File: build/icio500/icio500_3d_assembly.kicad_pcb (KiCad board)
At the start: 4 copper layers, 150.8 x 114.3 mm, 57 parts, among them J1 ?, U1 ?, U2 ?, U3 ?, U4 ?, U5 ?, U6 ?

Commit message: idk
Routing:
- net audio_in_r: track 108.5 -> 19.5 mm, vias 3 -> 0
- net gpio_disp_dc: track 76.4 -> 0.76 mm, vias 3 -> 0
- net gnd: track 235.5 -> 160.7 mm, vias 25 -> 22
- net i2c1_scl: track 74.9 -> 1.02 mm, vias 3 -> 0
- net gpio_disp_res: track 76.9 -> 3.48 mm, vias 3 -> 0
- net spi1_sck: track 69.8 -> 0.00 mm, vias 3 -> 0
- net i2c1_sda: track 70.3 -> 0.73 mm, vias 3 -> 0
- net spi1_cs: track 69.8 -> 0.98 mm, vias 3 -> 0
- net spi1_mosi: track 67.8 -> 1.14 mm, vias 3 -> 0
- net spi1_miso: track 63.7 -> 2.81 mm, vias 3 -> 0
- net gpio_enc_b: track 59.1 -> 30.5 mm, vias 3 -> 1
- net gpio_enc_sw: track 60.0 -> 34.9 mm, vias 3 -> 1
- net d13: track 55.7 -> 32.4 mm, vias 3 -> 1
- net d14: track 56.4 -> 33.7 mm, vias 3 -> 1
- net daisy_5v_power: track 155.1 -> 133.7 mm, vias 3 -> 1

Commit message: multistep error check and fixing
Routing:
- net i2c1_sda: track 0.73 -> 124.5 mm, vias 0 -> 3
- net i2c1_scl: track 1.02 -> 122.5 mm, vias 0 -> 3
- net spi1_mosi: track 1.14 -> 115.4 mm, vias 0 -> 3
- net spi1_sck: track 0.00 -> 114.0 mm, vias 0 -> 3
- net gpio_disp_dc: track 0.76 -> 112.5 mm, vias 0 -> 3
- net spi1_cs: track 0.98 -> 106.9 mm, vias 0 -> 3
- net spi1_miso: track 2.81 -> 108.3 mm, vias 0 -> 3
- net gpio_disp_res: track 3.48 -> 105.4 mm, vias 0 -> 3
- net d13: track 32.4 -> 113.8 mm, vias 1 -> 3
- net gpio_enc_b: track 30.5 -> 110.2 mm, vias 1 -> 3
- net d14: track 33.7 -> 105.6 mm, vias 1 -> 3
- net gpio_enc_sw: track 34.9 -> 102.0 mm, vias 1 -> 3
- net audio_in_r: track 19.5 -> 86.1 mm, vias 0 -> 3
- net gnd: track 160.7 -> 127.7 mm, vias 22 -> 28
- net daisy_5v_power: track 133.7 -> 135.0 mm, vias 1 -> 2

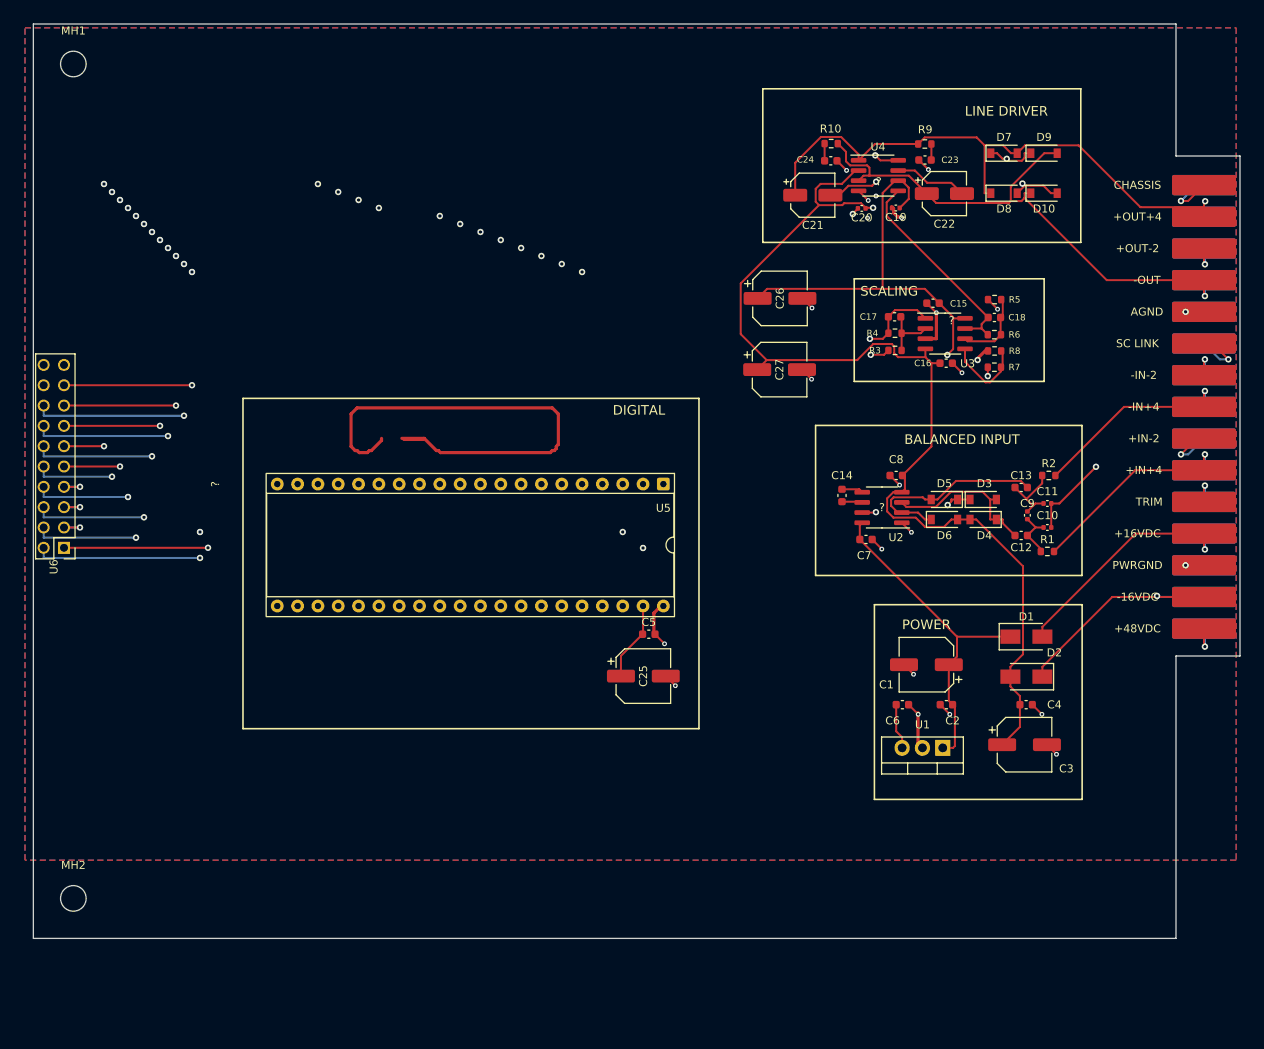
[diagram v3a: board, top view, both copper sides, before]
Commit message: Restore VPR summer board outline (Y=160mm, 26mm bottom notch), align lower bracket BR2, purge vestigial files
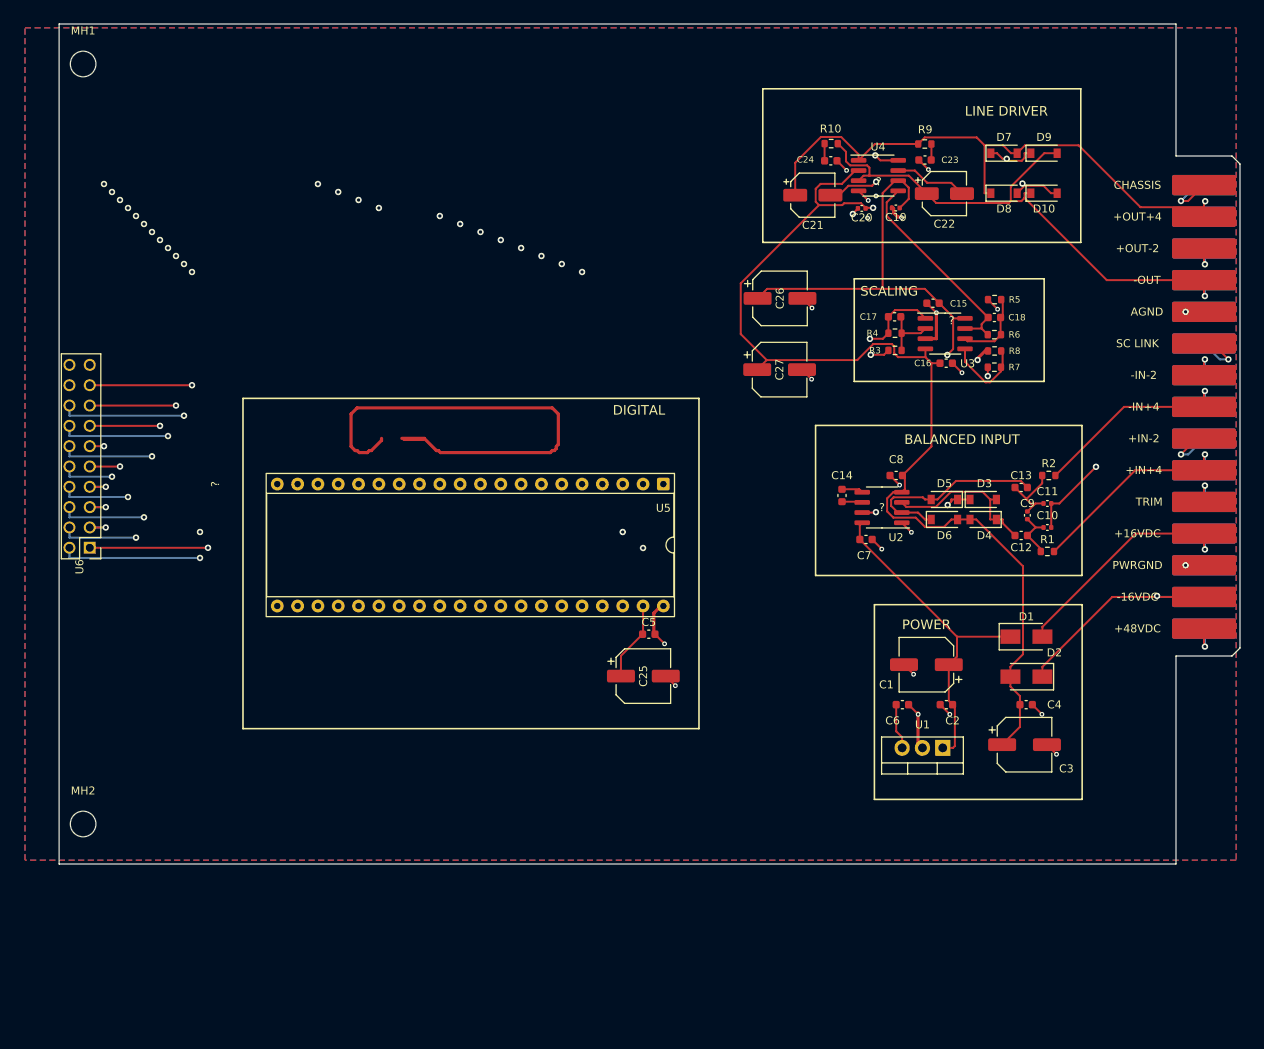
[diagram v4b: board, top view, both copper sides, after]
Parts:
- moved MH2 9.38 mm to (58.4, 155.0)
- moved U6 3.22 mm to (59.2, 120.5)
- moved ? 3.22 mm to (55.4, 112.2)
- moved MH1 1.22 mm to (58.4, 60.0)
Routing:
- net spi1_sck: track 114.0 -> 110.7 mm
- net spi1_mosi: track 115.4 -> 112.2 mm
- net spi1_miso: track 108.3 -> 105.1 mm
- net spi1_cs: track 106.9 -> 103.7 mm
- net i2c1_sda: track 124.5 -> 121.3 mm
- net i2c1_scl: track 122.5 -> 119.3 mm
- net gpio_enc_sw: track 102.0 -> 98.8 mm
- net gpio_enc_b: track 110.2 -> 107.0 mm
- net gpio_disp_res: track 105.4 -> 102.2 mm
- net daisy_5v_power: track 135.0 -> 131.8 mm
- net d14: track 105.6 -> 102.4 mm
- net d13: track 113.8 -> 110.6 mm
- net audio_in_r: track 86.1 -> 82.9 mm
- net gpio_disp_dc: track 112.5 -> 109.3 mm
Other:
- board size 150.8 x 114.3 mm -> 147.6 x 105 mm
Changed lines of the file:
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@@
 	(footprint "MountingHole_3.2mm_M3"
 		(layer "F.Cu")
-		(at 57.17 164.3)
+		(at 58.39 155)
 		(descr "Mounting Hole 3.2mm, M3, no annular, generated by kicad-footprint-generator mountinghole.py")
 		(tags "mountinghole M3")
@@
 	(footprint "Connector_PinHeader_2.54mm:PinHeader_2x10_P2.54mm_Horizontal"
 		(layer "F.Cu")
-		(at 56 120.475 180)
+		(at 59.22 120.47 180)
 		(descr "Through hole straight pin header, 2x10, 2.54mm pitch, double rows")
 		(tags "Through hole pin header THT 2x10 2.54mm double row")
@@
 	(footprint "MountingHole_3.2mm_M3"
 		(layer "F.Cu")
-		(at 57.17 60)
+		(at 58.39 60)
 		(descr "Mounting Hole 3.2mm, M3, no annular, generated by kicad-footprint-generator mountinghole.py")
 		(tags "mountinghole M3")
@@
 	)
 	(gr_line
-		(start 52.17 55)
+		(start 55.39 55)
 		(end 195 55)
 		(stroke
@@
 	)
 	(gr_line
-		(start 52.17 169.3)
-		(end 52.17 55)
+		(start 55.39 160)
+		(end 55.39 55)
 		(stroke
 			(width 0.1)
@@
 	(gr_line
 		(start 195 71.5)
-		(end 203 71.5)
+		(end 202 71.5)
 		(stroke
 			(width 0.1)
@@
 	(gr_line
 		(start 195 134)
-		(end 195 169.3)
+		(end 195 160)
 		(stroke
 			(width 0.1)
@@
 	)
 	(gr_line
-		(start 195 169.3)
-		(end 52.17 169.3)
+		(start 195 160)
+		(end 55.39 160)
 		(stroke
 			(width 0.1)
@@
 	)
 	(gr_line
-		(start 203 71.5)
-		(end 203 134)
+		(start 202 71.5)
+		(end 203 72.5)
 		(stroke
 			(width 0.1)
@@
 	)
 	(gr_line
-		(start 203 134)
+		(start 202 134)
 		(end 195 134)
 		(stroke
@@
 		(layer "Edge.Cuts")
 	)
+	(gr_line
+		(start 203 72.5)
+		(end 203 133)
+		(stroke
+			(width 0.1)
+			(type default)
+		)
+		(layer "Edge.Cuts")
+	)
+	(gr_line
+		(start 203 133)
+		(end 202 134)
+		(stroke
+			(width 0.1)
+			(type default)
+		)
+		(layer "Edge.Cuts")
+	)
 	(gr_text "DIGITAL"
 		(at 127.873162 103.2775 0)
@@
 	)
 	(segment
-		(start 56 120.475)
+		(start 59.22 120.475)
 		(end 74 120.475)
 		(width 0.25)
@@
 	)
 	(segment
-		(start 56 112.855)
-		(end 58 112.855)
+		(start 59.22 112.855)
+		(end 61.22 112.855)
 		(width 0.25)
 		(layer "F.Cu")
@@
 	)
 	(segment
-		(start 56 115.395)
-		(end 58 115.395)
+		(start 59.22 115.395)
+		(end 61.22 115.395)
 		(width 0.25)
 		(layer "F.Cu")
@@
 	)
 	(segment
-		(start 56 117.935)
-		(end 58 117.935)
+		(start 59.22 117.935)
+		(end 61.22 117.935)
 		(width 0.25)
 		(layer "F.Cu")
@@
 	)
 	(via
-		(at 58 117.935)
+		(at 61.22 117.935)
 		(size 0.8)
 		(drill 0.4)
@@
 	)
 	(via
-		(at 58 115.395)
+		(at 61.22 115.395)
 		(size 0.8)
 		(drill 0.4)
@@
 	)
 	(via
-		(at 58 112.855)
+		(at 61.22 112.855)
 		(size 0.8)
 		(drill 0.4)
@@
 	)
 	(segment
-		(start 56 115.395)
-		(end 58 115.395)
+		(start 59.22 115.395)
+		(end 61.22 115.395)
 		(width 0.25)
 		(layer "B.Cu")
@@
 	)
 	(segment
-		(start 56 112.855)
-		(end 58 112.855)
+		(start 59.22 112.855)
+		(end 61.22 112.855)
 		(width 0.25)
 		(layer "B.Cu")
@@
 	)
 	(segment
-		(start 56 117.935)
-		(end 58 117.935)
+		(start 59.22 117.935)
+		(end 61.22 117.935)
 		(width 0.25)
 		(layer "B.Cu")
@@
 	)
 	(segment
-		(start 56 100.155)
+		(start 59.22 100.155)
 		(end 72 100.155)
 		(width 0.25)
@@
 	)
 	(segment
-		(start 53.46 102.695)
-		(end 53.46 103.965)
+		(start 56.68 102.695)
+		(end 56.68 103.965)
 		(width 0.25)
 		(layer "B.Cu")
@@
 	)
 	(segment
-		(start 53.46 103.965)
+		(start 56.68 103.965)
 		(end 71 103.965)
 		(width 0.25)
@@
 	)
 	(segment
-		(start 56 102.695)
+		(start 59.22 102.695)
 		(end 70 102.695)
 		(width 0.25)
@@
 	)
 	(segment
-		(start 53.46 105.235)
-		(end 53.46 106.505)
+		(start 56.68 105.235)
+		(end 56.68 106.505)
 		(width 0.25)
 		(layer "B.Cu")
@@
 	)
 	(segment
-		(start 53.46 106.505)
+		(start 56.68 106.505)
 		(end 69 106.505)
 		(width 0.25)
@@
 	)
 	(segment
-		(start 56 105.235)
+		(start 59.22 105.235)
 		(end 68 105.235)
 		(width 0.25)
@@
 	)
 	(segment
-		(start 53.46 107.775)
-		(end 53.46 109.045)
+		(start 56.68 107.775)
+		(end 56.68 109.045)
 		(width 0.25)
 		(layer "B.Cu")
@@
 	)
 	(segment
-		(start 53.46 109.045)
+		(start 56.68 109.045)
 		(end 67 109.045)
 		(width 0.25)
@@
 	)
 	(segment
-		(start 53.46 116.665)
+		(start 56.68 116.665)
 		(end 66 116.665)
 		(width 0.25)
@@
 	)
 	(segment
-		(start 53.46 115.395)
-		(end 53.46 116.665)
+		(start 56.68 115.395)
+		(end 56.68 116.665)
 		(width 0.25)
 		(layer "B.Cu")
@@
 	)
 	(segment
-		(start 53.46 119.205)
+		(start 56.68 119.205)
 		(end 65 119.205)
 		(width 0.25)
@@
 	)
 	(segment
-		(start 53.46 117.935)
-		(end 53.46 119.205)
+		(start 56.68 117.935)
+		(end 56.68 119.205)
 		(width 0.25)
 		(layer "B.Cu")
@@
 	)
 	(segment
-		(start 53.46 112.855)
-		(end 53.46 114.125)
+		(start 56.68 112.855)
+		(end 56.68 114.125)
 		(width 0.25)
 		(layer "B.Cu")
@@
 	)
 	(segment
-		(start 53.46 114.125)
+		(start 56.68 114.125)
 		(end 64 114.125)
 		(width 0.25)
@@
 	)
 	(segment
-		(start 56 110.315)
+		(start 59.22 110.315)
 		(end 63 110.315)
 		(width 0.25)
@@
 	)
 	(segment
-		(start 53.46 111.585)
+		(start 56.68 111.585)
 		(end 62 111.585)
 		(width 0.25)
@@
 	)
 	(segment
-		(start 53.46 110.315)
-		(end 53.46 111.585)
+		(start 56.68 110.315)
+		(end 56.68 111.585)
 		(width 0.25)
 		(layer "B.Cu")
@@
 	)
 	(segment
-		(start 56 107.775)
+		(start 59.22 107.775)
 		(end 61 107.775)
 		(width 0.25)
@@
 	)
 	(segment
-		(start 53.46 121.745)
+		(start 56.68 121.745)
 		(end 73 121.745)
 		(width 0.25)
@@
 	)
 	(segment
-		(start 53.46 120.475)
-		(end 53.46 121.745)
+		(start 56.68 120.475)
+		(end 56.68 121.745)
 		(width 0.25)
 		(layer "B.Cu")
@@
 	(footprint "DUMMY"
 		(layer "F.Cu")
-		(at 52.17 112.15)
+		(at 55.39 112.15)
 		(attr exclude_from_pos_files exclude_from_bom)
 		(model "C:/Users/Chris Williams/Documents/GitHub/ICIO500/build/icio500/panel_satellite.step"
-			(offset (xyz -88.0 266.675 88.89))
+			(offset (xyz -0.08 166.675 -108.74))
 			(scale (xyz 1 1 1))
 			(rotate (xyz 0 90 0))
 		)
 		(model "C:/Users/Chris Williams/Documents/GitHub/ICIO500/build/icio500/faceplate_front.step"
-			(offset (xyz 0.0 66.675 -11.11))
+			(offset (xyz -1.68 66.675 -8.74))
 			(scale (xyz 1 1 1))
 			(rotate (xyz 0 90 0))

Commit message: Fix faceplate to approved minimalist aesthetic, fix 3D assembly offsets so header pins do not penetrate front panel
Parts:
- moved ? 3.22 mm to (52.2, 112.2)
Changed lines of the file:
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@@
 	(footprint "DUMMY"
 		(layer "F.Cu")
-		(at 55.39 112.15)
+		(at 52.17 112.15)
 		(attr exclude_from_pos_files exclude_from_bom)
 		(model "C:/Users/Chris Williams/Documents/GitHub/ICIO500/build/icio500/panel_satellite.step"
-			(offset (xyz -0.08 166.675 -108.74))
+			(offset (xyz -10.22 166.675 -108.74))
 			(scale (xyz 1 1 1))
 			(rotate (xyz 0 90 0))
 		)
 		(model "C:/Users/Chris Williams/Documents/GitHub/ICIO500/build/icio500/faceplate_front.step"
-			(offset (xyz -1.68 66.675 -8.74))
+			(offset (xyz -11.82 66.675 -8.74))
 			(scale (xyz 1 1 1))
 			(rotate (xyz 0 90 0))

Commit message: Rotate Daisy 90 deg CCW, route 0-DRC digital bus, and fix faceplate mechanical mating
- Restore Daisy Seed U5 vertical orientation (at 95 90 0) and DIGITAL silkscreen frame
- Route multilayer planar traces for all 12 U6-U5 digital nets, 5V power, and audio signals with 0 DRC violations and 0 unconnected items
- Fix 3D assembly offsets in scripts/make_assemblies.py for flush mating of main card, satellite board, and front faceplate
- Scale U6 3D model X axis to 0.5 to keep right-angle male pins seated inside socket J1 without faceplate protrusion
- Re-export JLCPCB fabrication packages and render assembly views
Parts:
- moved U5 42.4 mm to (95.0, 90.0), turned to 0 degrees
- moved ? 3.22 mm to (55.4, 112.2)
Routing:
- net i2c1_sda: track 121.3 -> 39.4 mm, vias 3 -> 0
- net i2c1_scl: track 119.3 -> 39.4 mm, vias 3 -> 0
- net gnd: track 127.7 -> 52.8 mm, vias 28 -> 25
- net spi1_mosi: track 112.2 -> 41.5 mm, vias 3 -> 0
- net spi1_sck: track 110.7 -> 40.4 mm, vias 3 -> 0
- net gpio_disp_dc: track 109.3 -> 39.4 mm, vias 3 -> 0
- net daisy_5v_power: track 131.8 -> 201.3 mm, vias 2 -> 0
- net spi1_miso: track 105.1 -> 37.9 mm, vias 3 -> 1
- net spi1_cs: track 103.7 -> 36.8 mm, vias 3 -> 0
- net gpio_disp_res: track 102.2 -> 35.8 mm, vias 3 -> 0
- net d13: track 110.6 -> 50.7 mm, vias 3 -> 2
- net d14: track 102.4 -> 47.6 mm, vias 3 -> 1
- net gpio_enc_sw: track 98.8 -> 46.3 mm, vias 3 -> 0
- net gpio_enc_b: track 107.0 -> 55.4 mm, vias 3 -> 2
- net audio_in_r: track 82.9 -> 123.0 mm, vias 3 -> 0
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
